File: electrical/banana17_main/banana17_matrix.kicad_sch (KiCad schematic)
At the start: 36 parts, among them SW1 SW, SW10 SW, SW11 SW, SW12 SW, SW13 SW, SW14 SW, SW15 SW, SW16 SW, SW17 SW, SW18 SW, SW2 SW, SW3 SW, SW4 SW, SW5 RotaryEncoder_Switch, SW6 SW, SW7 SW, SW8 SW, SW9 SW

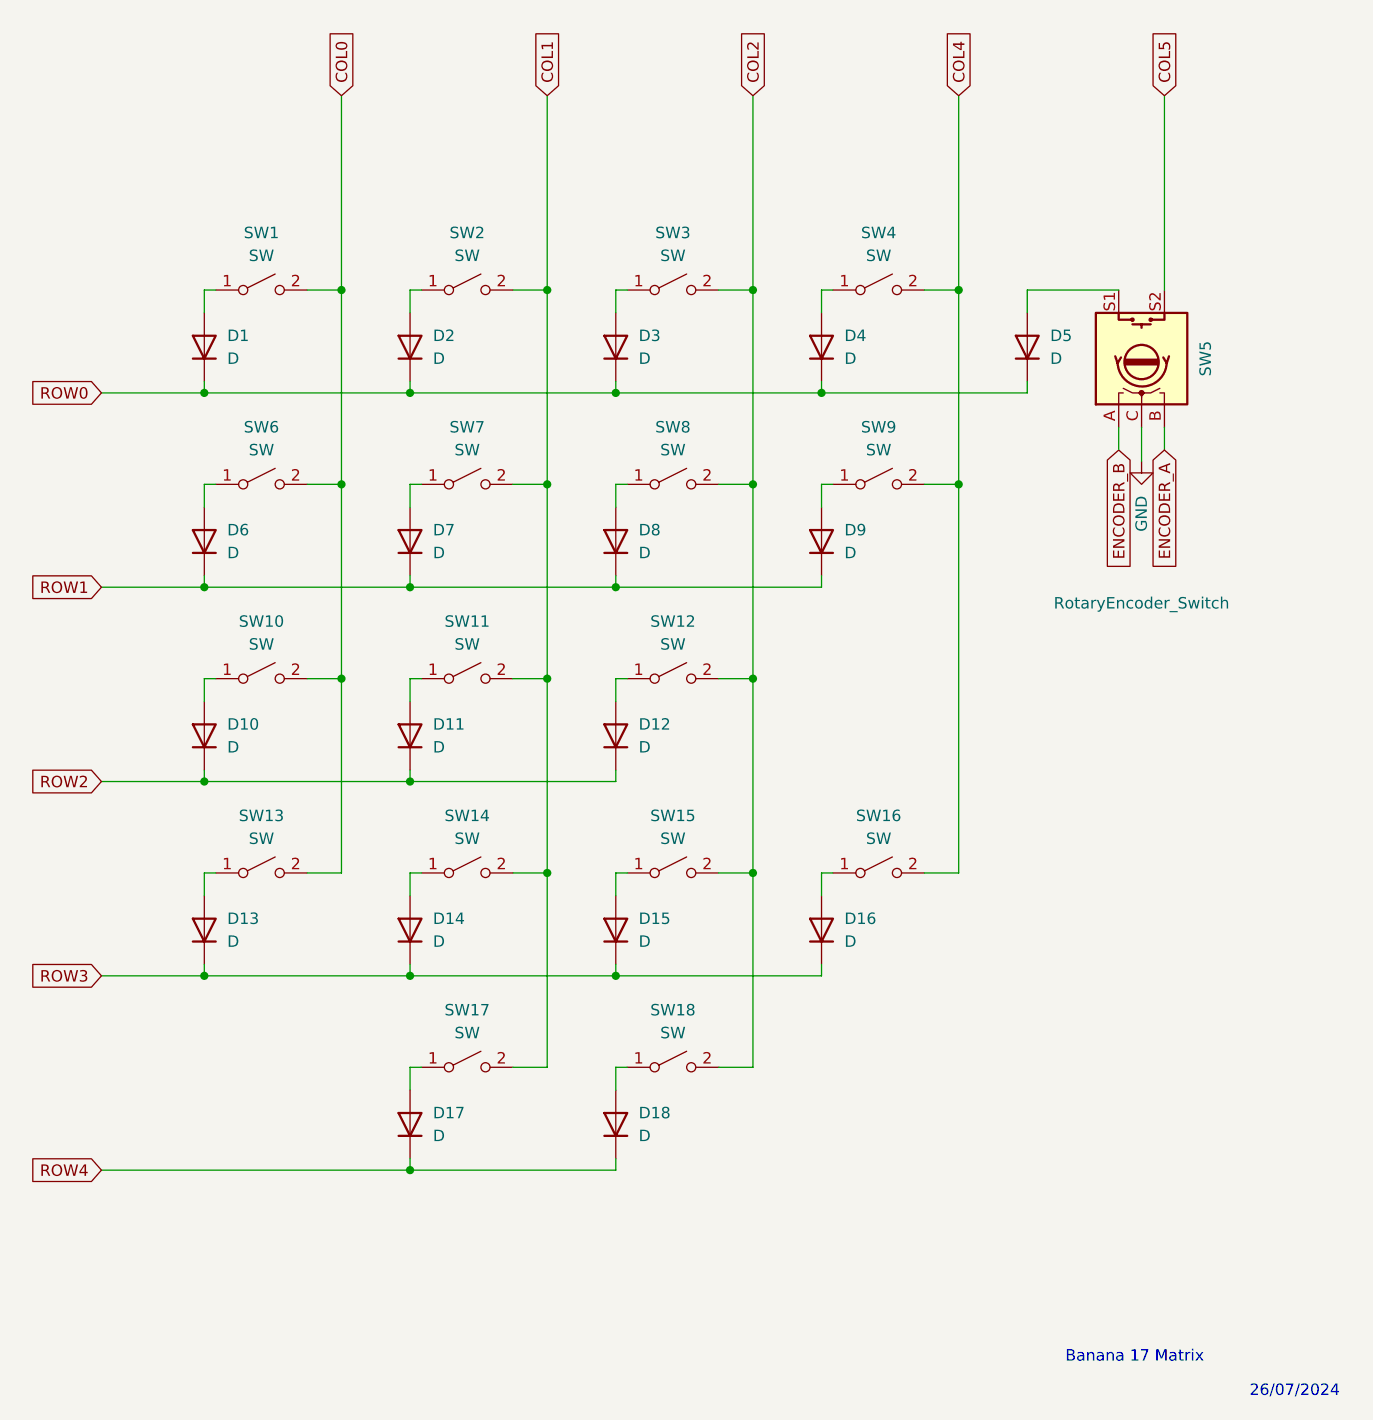
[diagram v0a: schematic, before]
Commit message: Reverted change for SSD1306 library import.
Reverted change for SSD1306 library import.
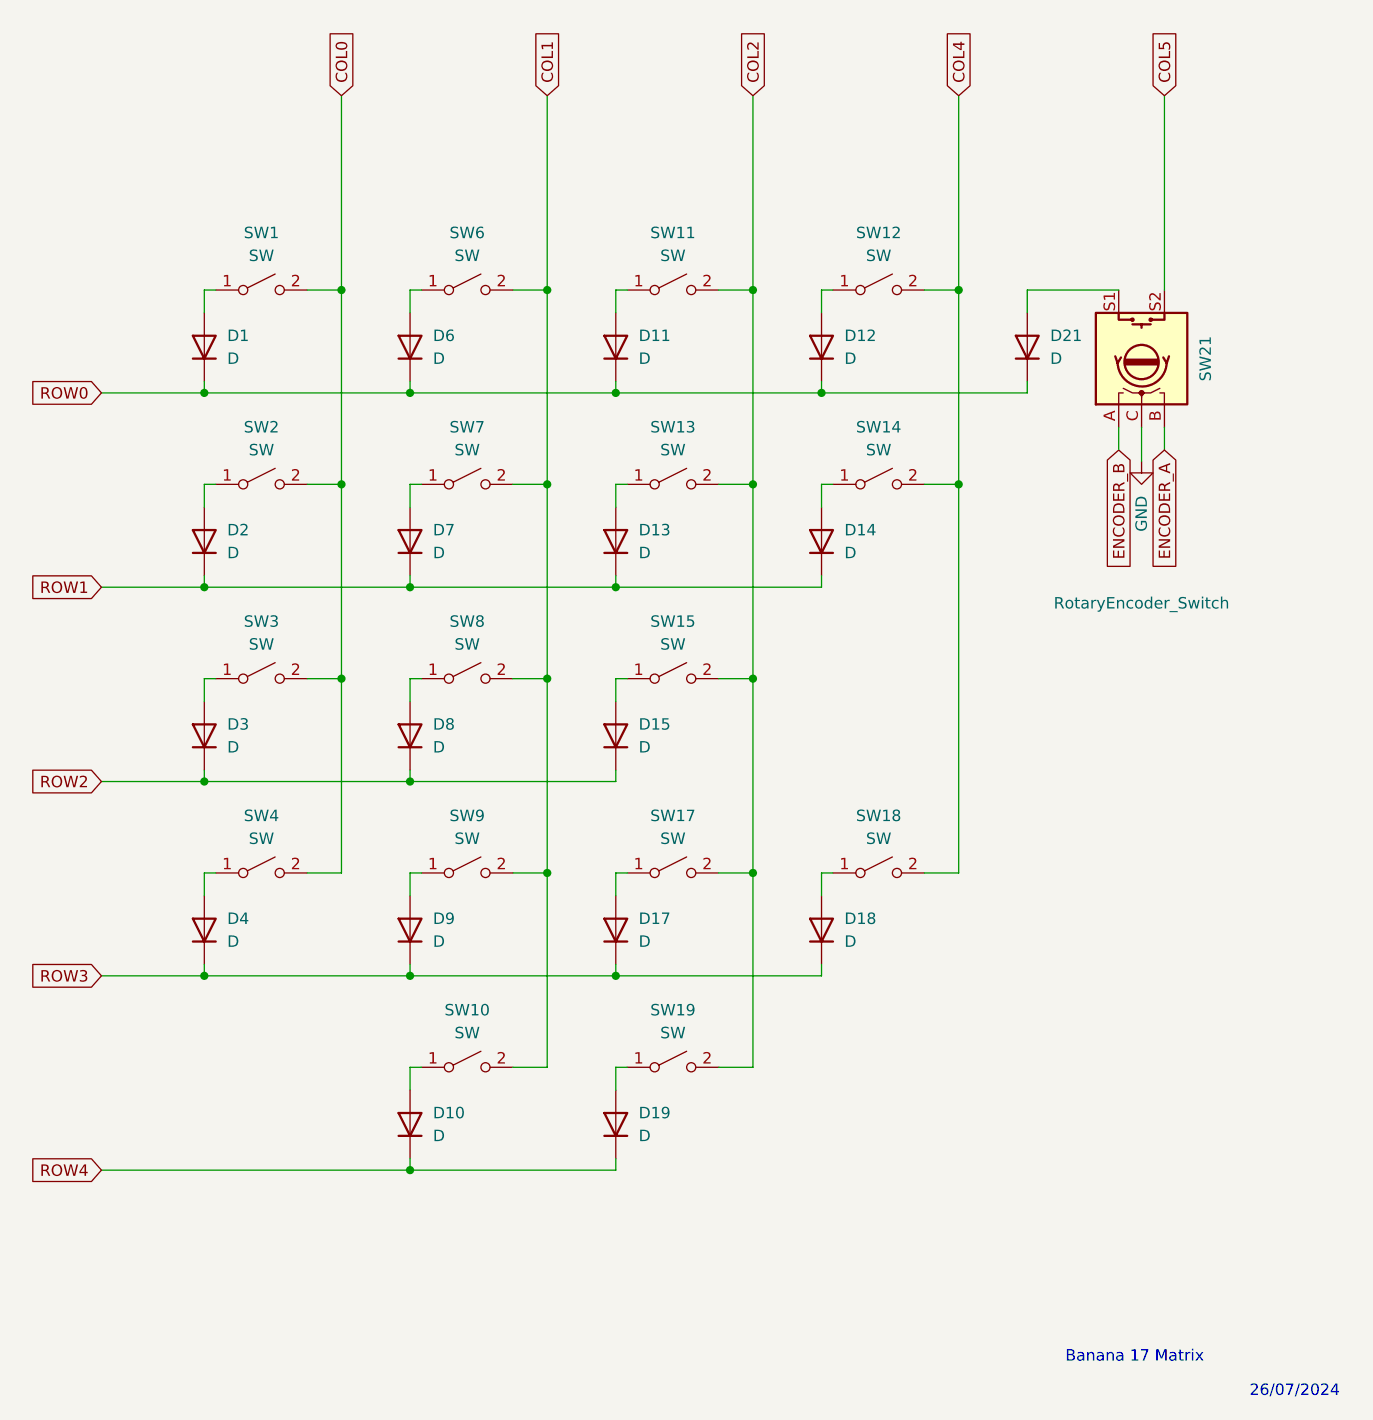
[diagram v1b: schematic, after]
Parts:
- renumbered D17 to D10, D3 to D11, D4 to D12, D8 to D13, D9 to D14, D12 to D15, D15 to D17, D16 to D18, D18 to D19, D6 to D2, D5 to D21, D10 to D3, D13 to D4, D2 to D6, D11 to D8, D14 to D9, SW17 to SW10, SW3 to SW11, SW4 to SW12, SW8 to SW13, SW9 to SW14, SW12 to SW15, SW15 to SW17, SW16 to SW18, SW18 to SW19, SW6 to SW2, SW5 to SW21, SW10 to SW3, SW13 to SW4, SW2 to SW6, SW11 to SW8, SW14 to SW9
